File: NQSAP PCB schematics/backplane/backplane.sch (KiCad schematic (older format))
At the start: 30 parts, among them J1 Bus, J10 Bus, J19 Conn_02x08, J2 Bus, J20 Conn_02x08, J21 Conn_02x08, J22 Conn_02x08, J23 Conn_02x08, J24 Conn_02x08, J25 Conn_02x08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

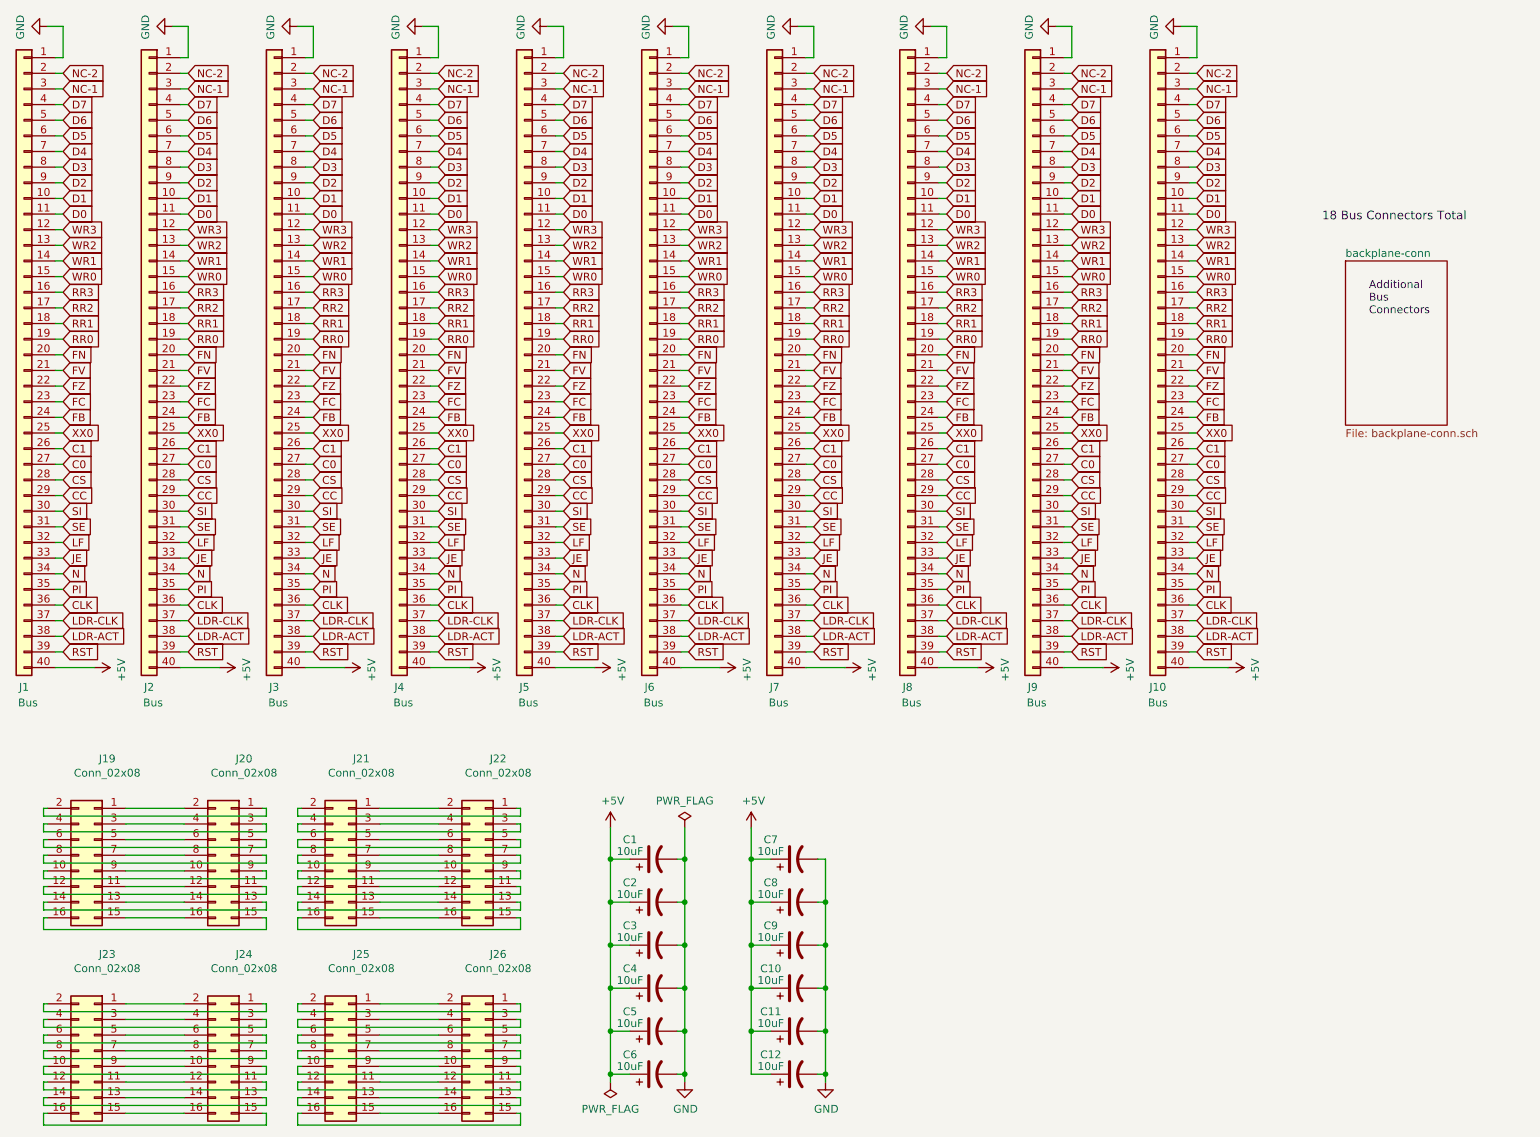
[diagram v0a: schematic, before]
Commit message: Add RAM, update and add gerbers for new boards
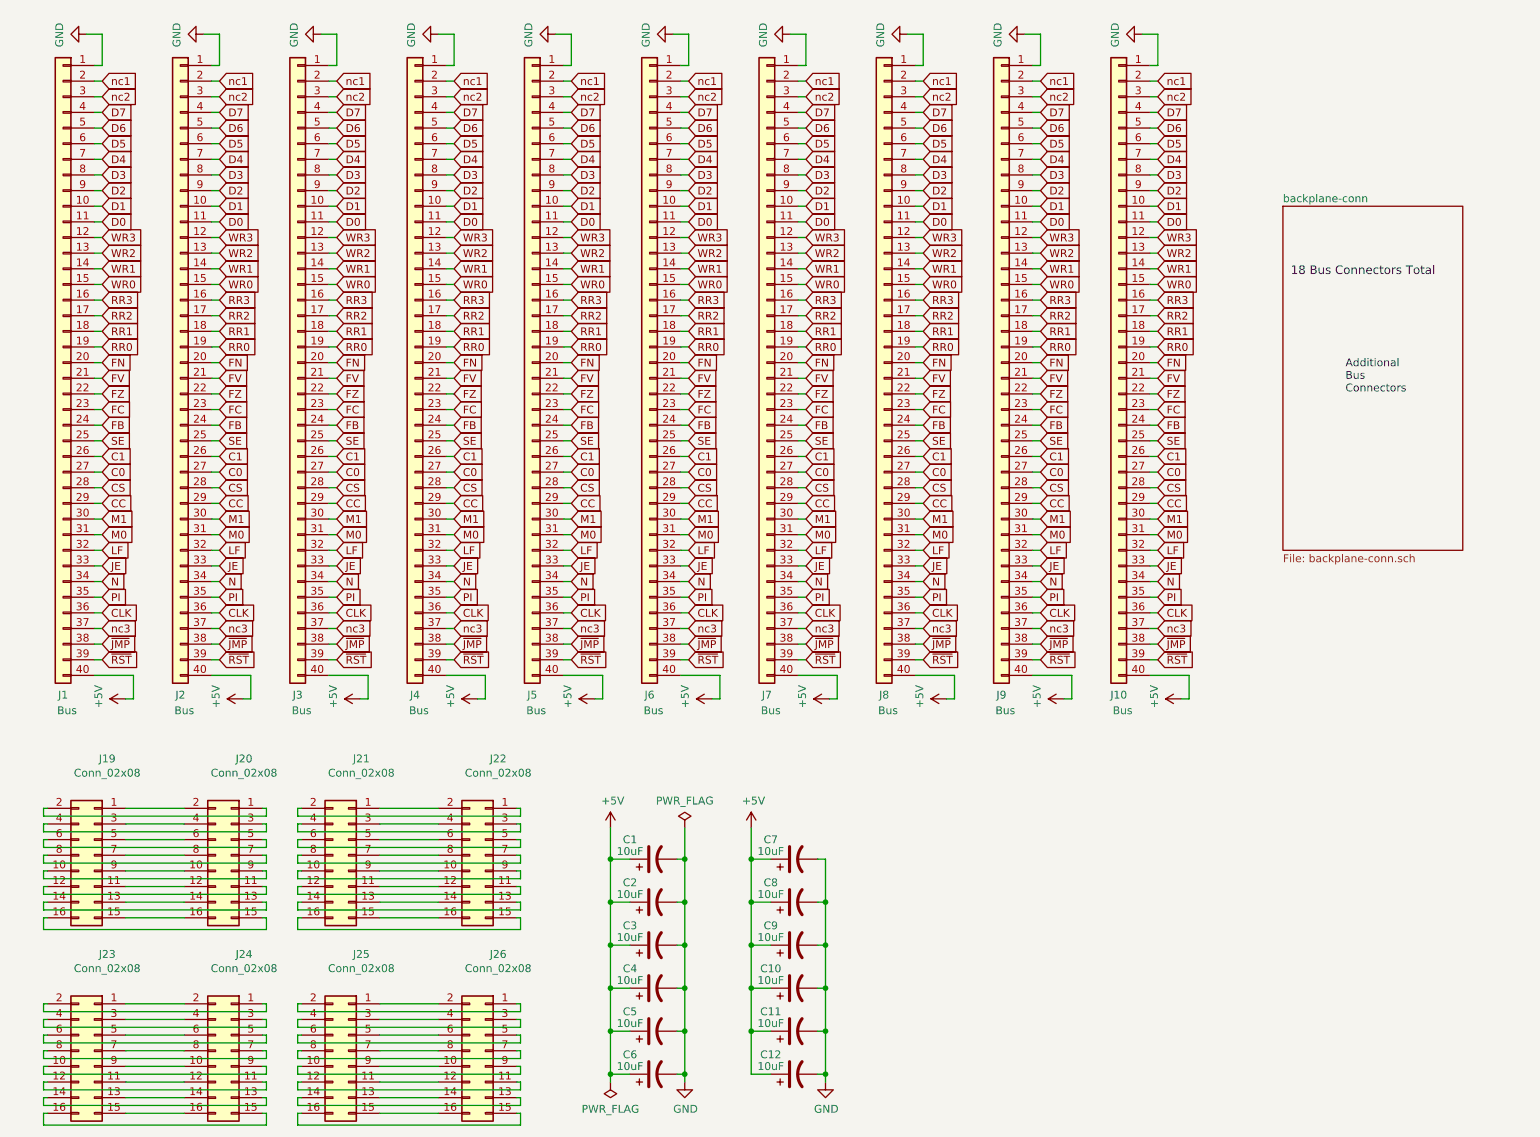
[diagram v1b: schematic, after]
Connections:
- net XX0 is gone; now on net SE: J1.25 (Pin_25), J10.25 (Pin_25), J2.25 (Pin_25), J3.25 (Pin_25), J4.25 (Pin_25), J5.25 (Pin_25), J6.25 (Pin_25), J7.25 (Pin_25), J8.25 (Pin_25), J9.25 (Pin_25)
- net SE: no longer J1.31 (Pin_31), J10.31 (Pin_31), J2.31 (Pin_31), J3.31 (Pin_31), J4.31 (Pin_31), J5.31 (Pin_31), J6.31 (Pin_31), J7.31 (Pin_31), J8.31 (Pin_31), J9.31 (Pin_31)
- net LDR-ACT renamed ~JMP
- net LDR-CLK renamed nc3
- net NC-1 renamed nc2
- net NC-2 renamed nc1
- net RST renamed ~RST
- net SI renamed M1
- new net M0: J1.31 (Pin_31), J10.31 (Pin_31), J2.31 (Pin_31), J3.31 (Pin_31), J4.31 (Pin_31), J5.31 (Pin_31), J6.31 (Pin_31), J7.31 (Pin_31), J8.31 (Pin_31), J9.31 (Pin_31)
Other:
- moved on the sheet: J1

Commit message: build 5 board updates
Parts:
- added J27, J28, J29, J30: POWER IN, TerminalBlock_RND:TerminalBlock_RND_205-00012_1x02_P5.00mm_Horizontal, symbol Connector:Screw_Terminal_01x02
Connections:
- net +5V: now also J27.2 (Pin_2), J28.2 (Pin_2), J29.1 (Pin_1), J30.1 (Pin_1)
- net GND: now also J27.1 (Pin_1), J28.1 (Pin_1), J29.2 (Pin_2), J30.2 (Pin_2)
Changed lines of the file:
@@
 Text GLabel 8050 4600 2    50   Input ~ 0
 ~JMP
+$Comp
+L Connector:Screw_Terminal_01x02 J29
+U 1 1 631BC50C
+P 9100 5950
+F 0 "J29" V 8972 6030 50  0000 L CNN
+F 1 "POWER IN" V 9200 5750 50  0000 L CNN
+F 2 "TerminalBlock_RND:TerminalBlock_RND_205-00012_1x02_P5.00mm_Horizontal" H 9100 5950 50  0001 C CNN
+F 3 "~" H 9100 5950 50  0001 C CNN
+	1    9100 5950
+	0    -1   1    0
+$EndComp
+$Comp
+L Connector:Screw_Terminal_01x02 J30
+U 1 1 63249C2B
+P 9100 6400
+F 0 "J30" V 8972 6480 50  0000 L CNN
+F 1 "POWER IN" V 9200 6200 50  0000 L CNN
+F 2 "TerminalBlock_RND:TerminalBlock_RND_205-00012_1x02_P5.00mm_Horizontal" H 9100 6400 50  0001 C CNN
+F 3 "~" H 9100 6400 50  0001 C CNN
+	1    9100 6400
+	0    -1   1    0
+$EndComp
+$Comp
+L Connector:Screw_Terminal_01x02 J27
+U 1 1 6324A5B5
+P 9200 4950
+F 0 "J27" V 9072 5030 50  0000 L CNN
+F 1 "POWER IN" V 9300 4750 50  0000 L CNN
+F 2 "TerminalBlock_RND:TerminalBlock_RND_205-00012_1x02_P5.00mm_Horizontal" H 9200 4950 50  0001 C CNN
+F 3 "~" H 9200 4950 50  0001 C CNN
+	1    9200 4950
+	0    1    -1   0
+$EndComp
+$Comp
+L Connector:Screw_Terminal_01x02 J28
+U 1 1 6324B1AF
+P 9200 5400
+F 0 "J28" V 9072 5480 50  0000 L CNN
+F 1 "POWER IN" V 9300 5200 50  0000 L CNN
+F 2 "TerminalBlock_RND:TerminalBlock_RND_205-00012_1x02_P5.00mm_Horizontal" H 9200 5400 50  0001 C CNN
+F 3 "~" H 9200 5400 50  0001 C CNN
+	1    9200 5400
+	0    1    -1   0
+$EndComp
+Wire Wire Line
+	9200 5600 9400 5600
+Wire Wire Line
+	9100 5750 8900 5750
+Wire Wire Line
+	9100 6200 8900 6200
+Wire Wire Line
+	9200 5150 9400 5150
+Wire Wire Line
+	9100 5600 8900 5600
+Wire Wire Line
+	9200 6200 9400 6200
+$Comp
+L power:+5V #PWR0103
+U 1 1 637E84D7
+P 8900 4900
+F 0 "#PWR0103" H 8900 4750 50  0001 C CNN
+F 1 "+5V" H 8915 5073 50  0000 C CNN
+F 2 "" H 8900 4900 50  0001 C CNN
+F 3 "" H 8900 4900 50  0001 C CNN
+	1    8900 4900
+	1    0    0    -1
+$EndComp
+$Comp
+L power:GND #PWR0104
+U 1 1 637E8B6A
+P 9400 6550
+F 0 "#PWR0104" H 9400 6300 50  0001 C CNN
+F 1 "GND" H 9405 6377 50  0000 C CNN
+F 2 "" H 9400 6550 50  0001 C CNN
+F 3 "" H 9400 6550 50  0001 C CNN
+	1    9400 6550
+	1    0    0    -1
+$EndComp
+Wire Wire Line
+	9100 5150 8900 5150
+Connection ~ 9400 6200
+Wire Wire Line
+	9400 6200 9400 6550
+Wire Wire Line
+	9400 5150 9400 5600
+Connection ~ 8900 5600
+Wire Wire Line
+	8900 5600 8900 5750
+Connection ~ 9400 5600
+Wire Wire Line
+	9400 5600 9400 5750
+Wire Wire Line
+	8900 4900 8900 5150
+Connection ~ 8900 5150
+Wire Wire Line
+	8900 5150 8900 5600
+Connection ~ 8900 5750
+Connection ~ 9400 5750
+Wire Wire Line
+	8900 5750 8900 6200
+Wire Wire Line
+	9400 5750 9400 6200
+Wire Wire Line
+	9200 5750 9400 5750
 $EndSCHEMATC
